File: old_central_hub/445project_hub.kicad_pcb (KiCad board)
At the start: 2 copper layers, 100 x 100 mm, 105 parts, among them J101 Barrel_Jack_Switch, J102 USB_B, J103 USB, J104 USB, J201 Conn_01x04, J202 Conn_01x04, J203 Conn_02x05_Odd_Even, J204 Conn_02x05_Odd_Even, J205 Conn_01x04, J206 Conn_02x05_Odd_Even, SW101 SW_Push, U101 MCP1826S, U102 SN75240, U103 TUSB2077A, U104 SN75240, U105 SN75240, U201 MCP2221AxSL, U202 MCP2221AxSL, U203 MCP2221AxSL, Y101 6MHz

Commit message: Central Hub rev. 1.1
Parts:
- J101: footprint Connector_BarrelJack:BarrelJack_CUI_PJ-102AH_Horizontal -> Connector_BarrelJack:BarrelJack_Horizontal
- moved J101 0.60 mm to (83.8, 54.8), turned to 0 degrees
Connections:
- U103 pad 10: GND -> +3V3
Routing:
- net GND: track 131.9 -> 127.8 mm
- net +5V: track 313.0 -> 314.5 mm
- net +3V3: track 112.7 -> 113.2 mm
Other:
- board text added: "Central Hub"
- board text added: "Rev. 1.1 2021.12.12"
- board text removed: "Team 15 - Central Hub"

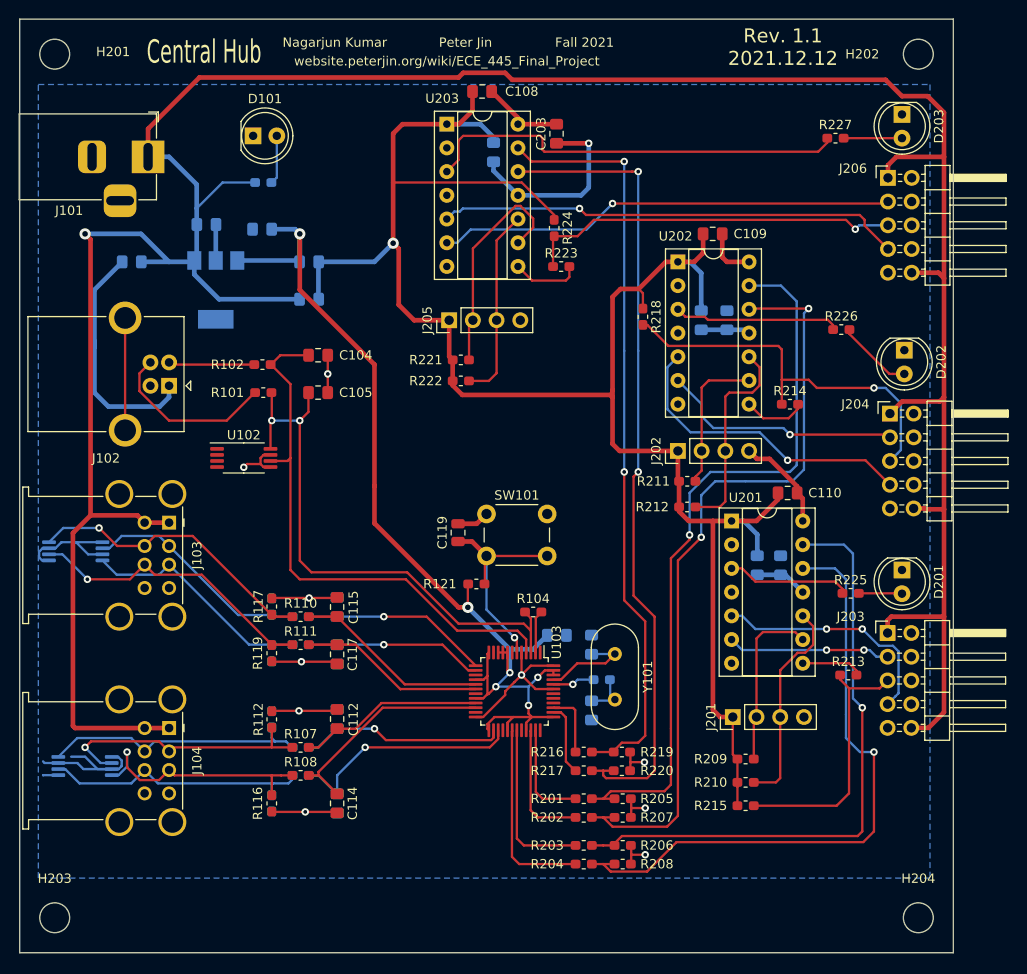
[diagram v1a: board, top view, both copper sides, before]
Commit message: Add capacitors on central hub
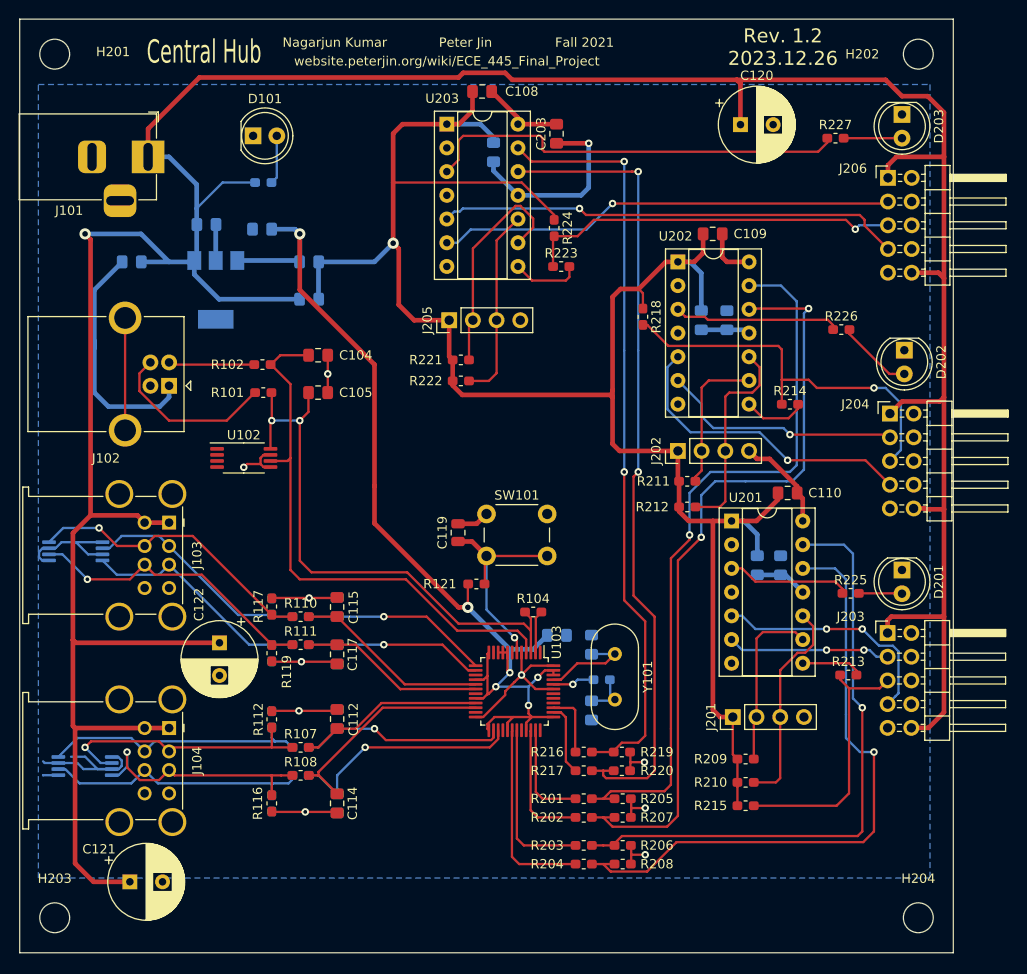
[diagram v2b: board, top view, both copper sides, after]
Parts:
- added C120: C_Polarized, Capacitor_THT:CP_Radial_D8.0mm_P3.50mm, F.Cu at (147.2, 51.3)
- added C121: C_Polarized, Capacitor_THT:CP_Radial_D8.0mm_P3.50mm, F.Cu at (81.8, 132.4)
- added C122: C_Polarized, Capacitor_THT:CP_Radial_D8.0mm_P3.50mm, F.Cu at (91.4, 106.8)
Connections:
- J101 pad 3: Net-(J101-Pad3) -> unconnected-(J101-Pad3)
- J102 pad 5: Net-(J102-Pad5) -> unconnected-(J102-Pad5)
- J203 pad 4: Net-(J203-Pad4) -> unconnected-(J203-Pad4)
- J203 pad 8: Net-(J203-Pad8) -> unconnected-(J203-Pad8)
- J204 pad 4: Net-(J204-Pad4) -> unconnected-(J204-Pad4)
- J204 pad 8: Net-(J204-Pad8) -> unconnected-(J204-Pad8)
- J206 pad 4: Net-(J206-Pad4) -> unconnected-(J206-Pad4)
- J206 pad 8: Net-(J206-Pad8) -> unconnected-(J206-Pad8)
- U103 pad 1: Net-(U103-Pad1) -> unconnected-(U103-Pad1)
- U103 pad 11: Net-(U103-Pad11) -> unconnected-(U103-Pad11)
- U103 pad 15: Net-(U103-Pad15) -> unconnected-(U103-Pad15)
- U103 pad 19: Net-(U103-Pad19) -> unconnected-(U103-Pad19)
- U103 pad 23: Net-(U103-Pad23) -> unconnected-(U103-Pad23)
- U103 pad 28: Net-(U103-Pad28) -> unconnected-(U103-Pad28)
- U103 pad 32: Net-(U103-Pad32) -> unconnected-(U103-Pad32)
- U103 pad 36: Net-(U103-Pad36) -> unconnected-(U103-Pad36)
- U103 pad 40: Net-(U103-Pad40) -> unconnected-(U103-Pad40)
- U103 pad 41: Net-(U103-Pad41) -> unconnected-(U103-Pad41)
- U103 pad 42: Net-(U103-Pad42) -> unconnected-(U103-Pad42)
- U103 pad 7: Net-(U103-Pad7) -> unconnected-(U103-Pad7)
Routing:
- net +5V: track 314.5 -> 356.5 mm
- net unconnected-(J102-Pad5): track 0.00 -> 12.0 mm
- net Net-(J102-Pad5): track 12.0 -> 0.00 mm
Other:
- net class Default removed
- board text added: "Rev. 1.2 2023.12.26"
- board text removed: "Rev. 1.1 2021.12.12"

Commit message: Make +5V traces thicker on old central hub
Due to the fact that there is no longer a chip shortage, the first
central hub will be used as the "primary" hub. The I2C devices (GPIO
expander, DS2482-100, real time clock, etc.) have moved onto the I2C
Sampler PCB in the IoTether repository.
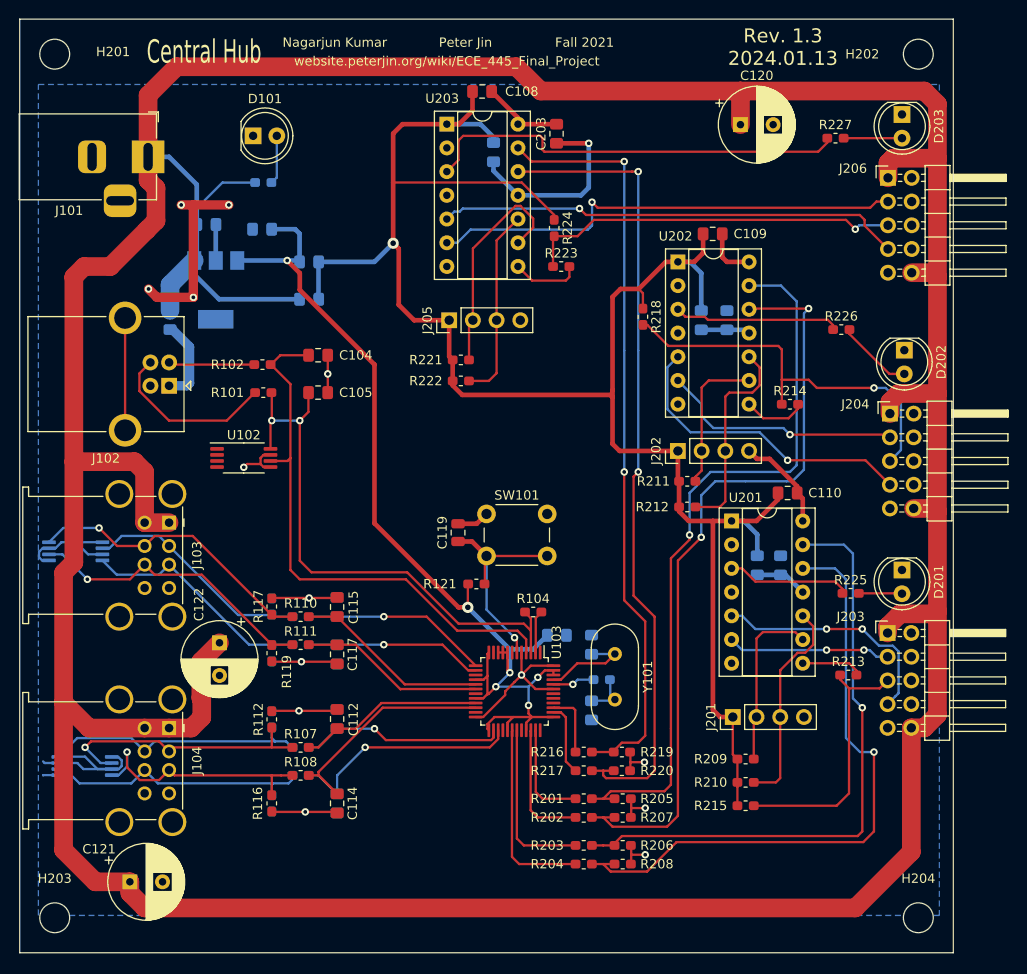
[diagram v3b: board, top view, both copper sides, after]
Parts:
- moved JP101 7.45 mm to (86.1, 72.2), turned to 90 degrees
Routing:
- net +5V: track 356.5 -> 466.8 mm, vias 1 -> 0
- net GND: track 127.8 -> 148.0 mm, vias 10 -> 14
- net Net-(J102-Pad1): track 26.2 -> 9.08 mm
- net +3V3: track 113.2 -> 110.9 mm
- net Net-(J206-Pad3): track 49.1 -> 51.3 mm
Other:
- board text added: "Rev. 1.3 2024.01.13"
- board text removed: "Rev. 1.2 2023.12.26"

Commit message: Add 12V->5V converter
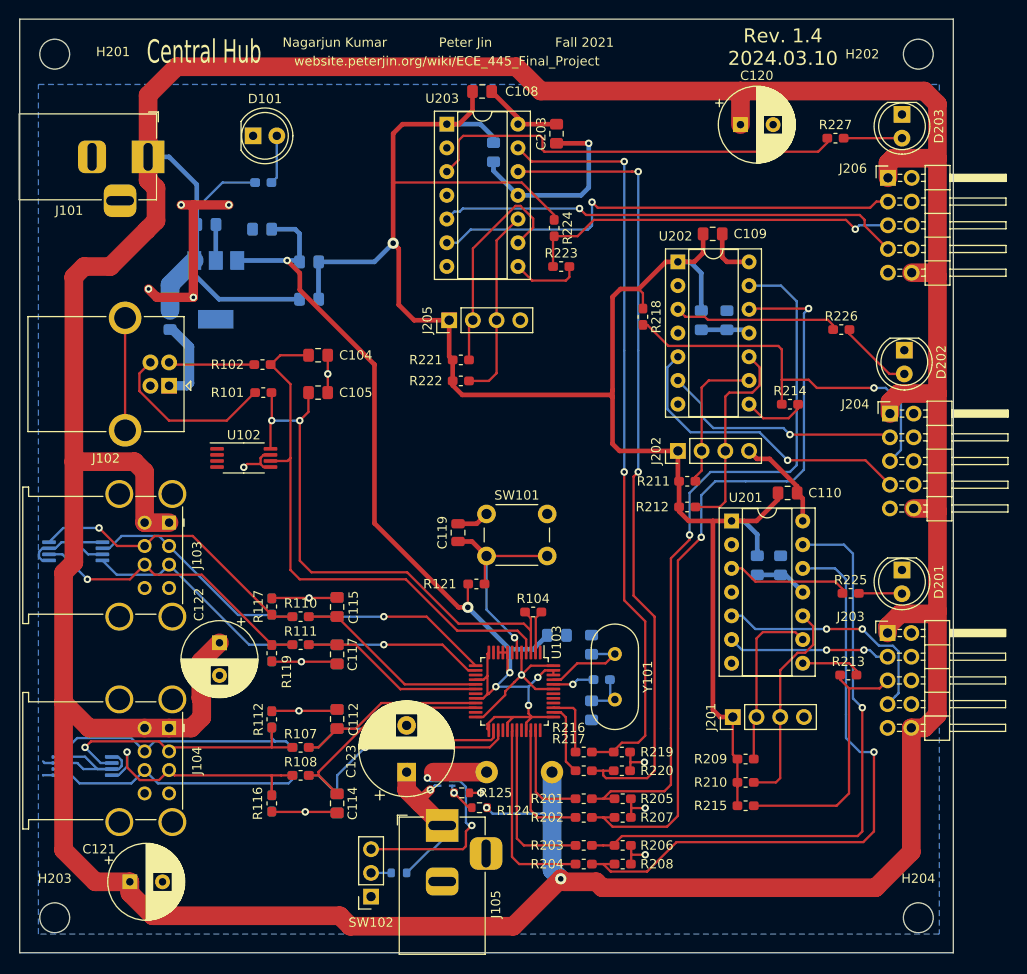
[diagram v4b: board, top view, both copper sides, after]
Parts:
- added C123: C_Polarized, Capacitor_THT:CP_Radial_D10.0mm_P5.00mm, F.Cu at (111.4, 120.7)
- added J105: Barrel_Jack_Switch, Connector_BarrelJack:BarrelJack_Horizontal, F.Cu at (115.3, 126.4)
- added J106: Conn_02x03_Counter_Clockwise, Package_TO_SOT_SMD:SOT-563, B.Cu at (115.6, 121.6)
- added L101: L, Inductor_THT:L_Radial_D12.5mm_P7.00mm_Fastron_09HCP, B.Cu at (120.0, 120.7)
- added R123: R, Resistor_SMD:R_0603_1608Metric, B.Cu at (110.6, 131.4)
- added R124: R, Resistor_SMD:R_0603_1608Metric, F.Cu at (119.3, 124.5)
- added R125: R, Resistor_SMD:R_0603_1608Metric, F.Cu at (117.3, 122.9)
- added SW102: SW_SPDT, Connector_PinSocket_2.54mm:PinSocket_1x03_P2.54mm_Vertical, F.Cu at (107.6, 134.0)
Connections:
- U201 pad 2: Net-(U201-Pad2) -> unconnected-(U201-Pad2)
- U201 pad 4: Net-(U201-Pad4) -> unconnected-(U201-Pad4)
- U201 pad 7: Net-(U201-Pad7) -> unconnected-(U201-Pad7)
- U202 pad 2: Net-(U202-Pad2) -> unconnected-(U202-Pad2)
- U202 pad 4: Net-(U202-Pad4) -> unconnected-(U202-Pad4)
- U202 pad 7: Net-(U202-Pad7) -> unconnected-(U202-Pad7)
- U203 pad 2: Net-(U203-Pad2) -> unconnected-(U203-Pad2)
- U203 pad 4: Net-(U203-Pad4) -> unconnected-(U203-Pad4)
- U203 pad 7: Net-(U203-Pad7) -> unconnected-(U203-Pad7)
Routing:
- net +5V: track 466.8 -> 488.7 mm, vias 0 -> 2
- net Net-(J106-Pad5): track 0.00 -> 19.1 mm, vias 0 -> 1
- net Net-(C123-Pad1): track 0.00 -> 17.1 mm, vias 0 -> 1
- net Net-(J106-Pad2): track 0.00 -> 7.90 mm, vias 0 -> 1
- net Net-(J106-Pad6): track 0.00 -> 3.42 mm, vias 0 -> 1
- net GND: track 148.0 -> 150.7 mm, vias 14 -> 15
- net Net-(R123-Pad2): track 0.00 -> 2.16 mm
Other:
- board text added: "Rev. 1.4 2024.03.10"
- board text removed: "Rev. 1.3 2024.01.13"
